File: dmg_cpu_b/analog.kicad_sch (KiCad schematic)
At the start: 20 parts

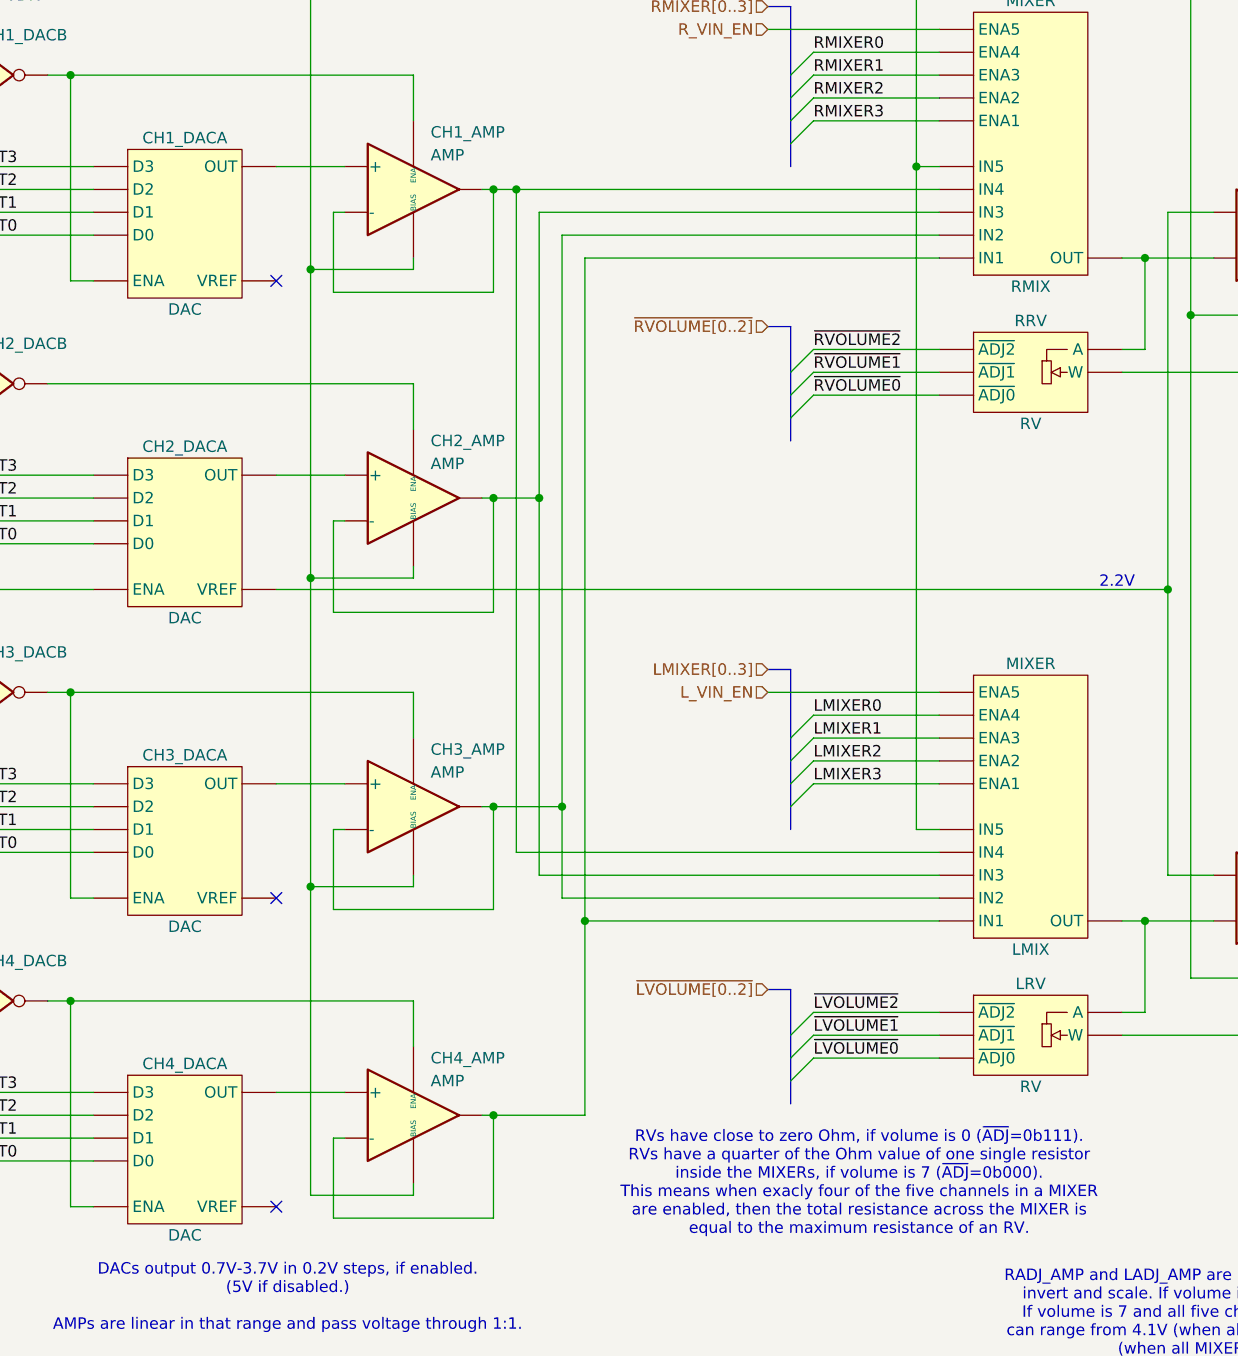
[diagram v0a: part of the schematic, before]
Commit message: Improve DAC and MIXER symbols
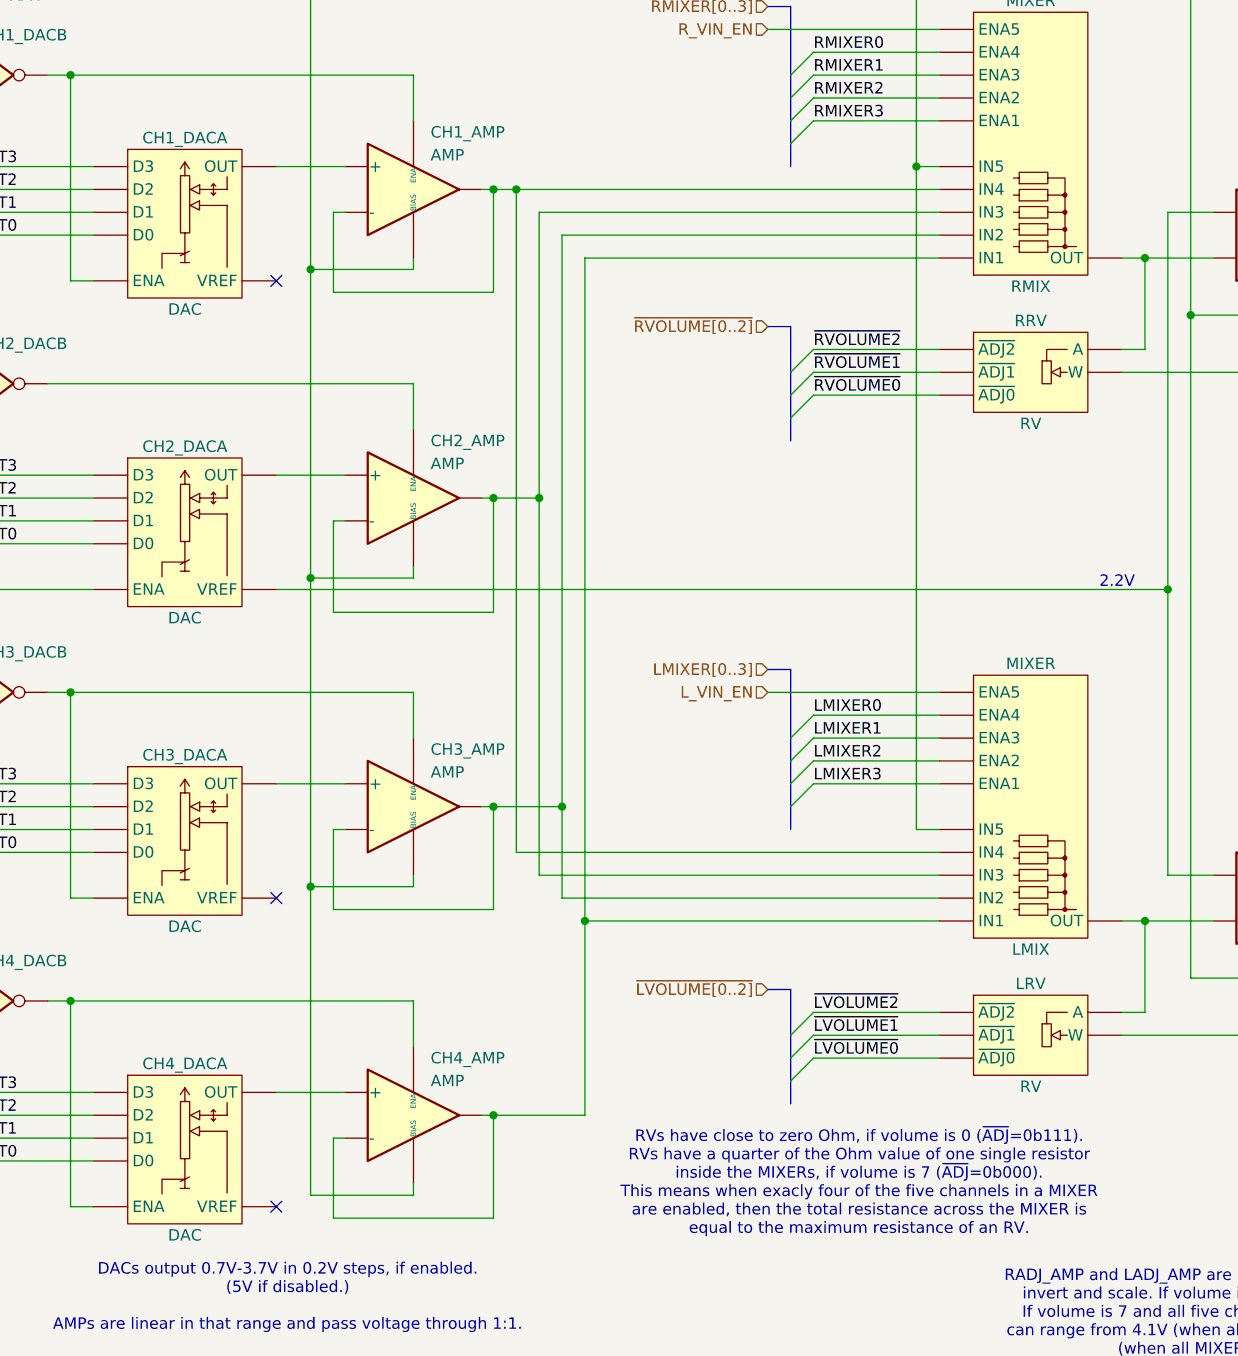
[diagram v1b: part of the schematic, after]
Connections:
- net at CH4_AMP.: now also LMIX. (OUT), RMIX. (OUT); no longer CH4_DAC. (VREF)
- net at CH1_AMP.: now also LMIX. (OUT), RMIX. (OUT); no longer CH1_DAC. (VREF)
- net at CH3_AMP.: now also LMIX. (OUT), RMIX. (OUT); no longer CH3_DAC. (VREF)
- net at CH2_AMP.: now also LMIX. (OUT), RMIX. (OUT); no longer CH2_DAC.
- new net: CH1_AMP., CH2_AMP., CH3_AMP., CH4_AMP., LADJ_AMP., LOUT_AMP., RADJ_AMP., ROUT_AMP., VDIV. (VREF)
- new net: LADJ_AMP., LOUT_AMP., LRV. (W)
- new net: LMIX. (OUT), RMIX. (OUT), VIN.1 (A)
- new net: CH4_AMP., CH4_DAC. (VREF)
- new net: CH4_AMP., CH4_DAC., CH4_DAC. (VREF)
- new net: CH1_AMP., CH1_DAC., CH1_DAC. (VREF)
- new net: CH1_AMP., CH1_DAC. (VREF)
- new net: CH3_AMP., CH3_DAC., CH3_DAC. (VREF)
- new net: CH3_AMP., CH3_DAC. (VREF)
- new net: LADJ_AMP., LMIX. (OUT), LRV. (W)
- new net: CH2_DAC. (VREF), LADJ_AMP., RADJ_AMP.
- new net: CH2_AMP., CH2_DAC.
- new net: RADJ_AMP., RMIX. (OUT), RRV. (W)
- new net: RADJ_AMP., ROUT_AMP., RRV. (W)
- new net: CH2_AMP., CH2_DAC. (VREF)
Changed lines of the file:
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@@
 	)
 	(symbol
+		(lib_name "DAC_5")
 		(lib_id "DMG_CPU_Cells:DAC")
 		(at 123.19 104.14 0)
@@
 	)
 	(symbol
-		(lib_name "DAC_6")
+		(lib_name "DAC_2")
 		(lib_id "DMG_CPU_Cells:DAC")
 		(at 123.19 172.72 0)
@@
 	)
 	(symbol
-		(lib_name "DAC_5")
+		(lib_name "DAC_6")
 		(lib_id "DMG_CPU_Cells:DAC")
 		(at 123.19 207.01 0)
@@
 	)
 	(symbol
-		(lib_name "DAC_2")
 		(lib_id "DMG_CPU_Cells:DAC")
 		(at 123.19 138.43 0)

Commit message: Release revision 0.11 of both schematics
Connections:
- net at CH4_AMP.: now also LMIX. (OUT), RMIX. (OUT); no longer CH4_DAC. (VREF)
- net at CH1_AMP.: now also LMIX. (OUT), RMIX. (OUT); no longer CH1_DAC. (VREF)
- net at CH3_AMP.: now also LMIX. (OUT), RMIX. (OUT); no longer CH3_DAC. (VREF)
- net at CH2_AMP.: now also LMIX. (OUT), RMIX. (OUT); no longer CH2_DAC.
- new net: CH1_AMP., CH2_AMP., CH3_AMP., CH4_AMP., LADJ_AMP., LOUT_AMP., RADJ_AMP., ROUT_AMP., VDIV. (VREF)
- new net: LADJ_AMP., LOUT_AMP., LRV. (W)
- new net: LMIX. (OUT), RMIX. (OUT), VIN.1 (A)
- new net: CH4_AMP., CH4_DAC. (VREF)
- new net: CH4_AMP., CH4_DAC., CH4_DAC. (VREF)
- new net: CH1_AMP., CH1_DAC., CH1_DAC. (VREF)
- new net: CH1_AMP., CH1_DAC. (VREF)
- new net: CH3_AMP., CH3_DAC., CH3_DAC. (VREF)
- new net: CH3_AMP., CH3_DAC. (VREF)
- new net: LADJ_AMP., LMIX. (OUT), LRV. (W)
- new net: CH2_DAC. (VREF), LADJ_AMP., RADJ_AMP.
- new net: CH2_AMP., CH2_DAC.
- new net: RADJ_AMP., RMIX. (OUT), RRV. (W)
- new net: RADJ_AMP., ROUT_AMP., RRV. (W)
- new net: CH2_AMP., CH2_DAC. (VREF)
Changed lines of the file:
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@@
 	(title_block
 		(title "DMG-CPU B")
-		(date "2026-03-22")
-		(rev "0.10")
+		(date "2026-04-11")
+		(rev "0.11")
 		(company "CC-BY-SA-4.0 Régis Galland & Michael Singer -- Derived work from Furrtek")
 		(comment 1 "https://github.com/msinger/dmg-schematics")

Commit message: Update amplifier description
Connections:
- net at CH4_AMP.: now also LMIX. (OUT), RMIX. (OUT); no longer CH4_DAC. (VREF)
- net at CH1_AMP.: now also LMIX. (OUT), RMIX. (OUT); no longer CH1_DAC. (VREF)
- net at CH3_AMP.: now also LMIX. (OUT), RMIX. (OUT); no longer CH3_DAC. (VREF)
- net at CH2_AMP.: now also LMIX. (OUT), RMIX. (OUT); no longer CH2_DAC.
- new net: CH1_AMP., CH2_AMP., CH3_AMP., CH4_AMP., LADJ_AMP., LOUT_AMP., RADJ_AMP., ROUT_AMP., VDIV. (VREF)
- new net: LADJ_AMP., LOUT_AMP., LRV. (W)
- new net: LMIX. (OUT), RMIX. (OUT), VIN.1 (A)
- new net: CH4_AMP., CH4_DAC. (VREF)
- new net: CH4_AMP., CH4_DAC., CH4_DAC. (VREF)
- new net: CH1_AMP., CH1_DAC., CH1_DAC. (VREF)
- new net: CH1_AMP., CH1_DAC. (VREF)
- new net: CH3_AMP., CH3_DAC., CH3_DAC. (VREF)
- new net: CH3_AMP., CH3_DAC. (VREF)
- new net: LADJ_AMP., LMIX. (OUT), LRV. (W)
- new net: CH2_DAC. (VREF), LADJ_AMP., RADJ_AMP.
- new net: CH2_AMP., CH2_DAC.
- new net: RADJ_AMP., RMIX. (OUT), RRV. (W)
- new net: RADJ_AMP., ROUT_AMP., RRV. (W)
- new net: CH2_AMP., CH2_DAC. (VREF)
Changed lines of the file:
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@@
 	(title_block
 		(title "DMG-CPU B")
-		(date "2026-04-11")
+		(date "2026-05-18")
 		(rev "0.11")
 		(company "CC-BY-SA-4.0 Régis Galland & Michael Singer -- Derived work from Furrtek")
@@
 	)
 	(symbol
-		(lib_name "AMP_1")
+		(lib_name "AMP_3")
 		(lib_id "DMG_CPU_Cells:AMP")
 		(at 275.59 181.61 0)
@@
 			)
 		)
-		(property "Description" "Audio amplifier."
+		(property "Description" "CMOS differential amplifier with push-pull output."
 			(at 275.59 190.5 0)
 			(effects
@@
 			)
 		)
-		(property "Description" "Audio amplifier."
+		(property "Description" "CMOS differential amplifier with push-pull output."
 			(at 148.59 212.09 0)
 			(effects
@@
 	)
 	(symbol
-		(lib_name "AMP_6")
+		(lib_name "AMP_2")
 		(lib_id "DMG_CPU_Cells:AMP")
 		(at 245.11 179.07 0)
@@
 			)
 		)
-		(property "Description" "Audio amplifier."
+		(property "Description" "CMOS differential amplifier with push-pull output."
 			(at 245.11 187.96 0)
 			(effects
@@
 	)
 	(symbol
-		(lib_name "AMP_2")
+		(lib_name "AMP_5")
 		(lib_id "DMG_CPU_Cells:AMP")
 		(at 148.59 100.33 0)
@@
 			)
 		)
-		(property "Description" "Audio amplifier."
+		(property "Description" "CMOS differential amplifier with push-pull output."
 			(at 148.59 109.22 0)
 			(effects
@@
 	)
 	(symbol
+		(lib_name "AMP_6")
 		(lib_id "DMG_CPU_Cells:AMP")
 		(at 245.11 105.41 0)
@@
 			)
 		)
-		(property "Description" "Audio amplifier."
+		(property "Description" "CMOS differential amplifier with push-pull output."
 			(at 245.11 114.3 0)
 			(effects
@@
 	)
 	(symbol
-		(lib_name "AMP_3")
+		(lib_name "AMP_1")
 		(lib_id "DMG_CPU_Cells:AMP")
 		(at 148.59 134.62 0)
@@
 			)
 		)
-		(property "Description" "Audio amplifier."
+		(property "Description" "CMOS differential amplifier with push-pull output."
 			(at 148.59 143.51 0)
 			(effects
@@
 	)
 	(symbol
-		(lib_name "AMP_5")
+		(lib_name "AMP_7")
 		(lib_id "DMG_CPU_Cells:AMP")
 		(at 275.59 107.95 0)
@@
 			)
 		)
-		(property "Description" "Audio amplifier."
+		(property "Description" "CMOS differential amplifier with push-pull output."
 			(at 275.59 116.84 0)
 			(effects
@@
 	)
 	(symbol
-		(lib_name "AMP_7")
 		(lib_id "DMG_CPU_Cells:AMP")
 		(at 148.59 168.91 0)
@@
 			)
 		)
-		(property "Description" "Audio amplifier."
+		(property "Description" "CMOS differential amplifier with push-pull output."
 			(at 148.59 177.8 0)
 			(effects
